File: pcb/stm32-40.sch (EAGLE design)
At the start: 83 parts, among them IC1 STM32F103RBT6, IC2 CAT24M01WI-GT3, IC3 MAX487-S, IC4 AMIS30663CANG2G, Q1 32768Hz, Q2 8MHz, SW1 KSS-2EG4430, SW2 KSS-2EG4430, X1 MCV3, X2 MCV3

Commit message: stamp + lcd
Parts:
- removed JP1: (no value), jtag:SWD-5_2.54
- removed STMP1: STAMP-40, stamp:STAMP-40
- added C13: 0.1, rc-master-smd:C_0603
- added LCD1: (no value), lcd1202:LCD1202-EXT
- added Q3: MMBT2222, semiconductor:MMBT2222
- added R37, R38, R39, R40, R43: 10, rc-master-smd:R_0603
- added R41, R42: 4.7K, rc-master-smd:R_0603
- added R44: 2K, rc-master-smd:R_0603
- added STMP2: STAMP-40, stamp:STAMP-40
- added SW3, SW4, SW5: KSS-2EG4430, buttons:KSS-2EG4430
- added SWD1: SWD-6, jtag:SWD-6
- G1: device battery:LI3VHOLDER -> battery:1220SMT
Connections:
- new net !LCD_CS: LCD1.!CS, R41.1
- new net BL: R44.2
- new net LCD_CLK: LCD1.SCLK
- new net LCD_DATA: LCD1.SI
- new net N$25: R37.1, STMP2G$1.6
- new net N$26: R38.1, STMP2G$1.5
- new net N$27: R39.1, STMP2G$1.4
- new net N$28: R40.1, STMP2G$1.3
- new net N$29: LCD1.LEDK, Q3.C
- new net N$31: LCD1.LEDA, R43.1
- new net N$32: Q3.B, R44.1
- new net PA15: IC1.JTDI/(TIM2_CH1_ETR/PA15/SPI1_NSS), STMP2G$2.4
- net !RESET: now also LCD1.!RST, R42.2, SWD1.5; no longer JP1.4
- net +3V3: now also C13.1, LCD1.VDD, LCD1.VDDI, R41.2, R43.2, SWD1.1; no longer JP1.1
- net +5V: now also STMP2G$1.1; no longer STMP1G$1.20
- net CAN_L: now also S1.8, X2.2.SK; no longer S1.1, X2.3.SK
- net GND: now also C13.2, LCD1.GND@3, LCD1.GND@8, Q3.E, R42.1, S1.5, S1.6, STMP2G$1.11, STMP2G$1.2, STMP2G$1.20, STMP2G$2.1, STMP2G$2.20, SW3.P, SW4.P, SW5.P, SWD1.3, X1.3.SK, X2.3.SK; no longer JP1.5, S1.3, S1.4, STMP1G$1.1, STMP1G$1.10, STMP1G$1.19, STMP1G$2.1, STMP1G$2.20, X1.2.SK, X2.2.SK
- net N$10: now also S1.4; no longer S1.5
- net N$11: now also STMP2G$1.10; no longer STMP1G$1.11
- net N$14: now also STMP2G$1.9; no longer STMP1G$1.12
- net N$15: now also STMP2G$1.19; no longer STMP1G$1.2
- net N$16: now also STMP2G$1.18; no longer STMP1G$1.3
- net N$17: now also STMP2G$1.17; no longer STMP1G$1.4
- net N$18: now also STMP2G$1.16; no longer STMP1G$1.5
- net N$19: now also STMP2G$1.15; no longer STMP1G$1.6
- net N$2: now also S1.1; no longer S1.8
- net N$20: now also STMP2G$1.14; no longer STMP1G$1.7
- net N$21: now also STMP2G$1.13; no longer STMP1G$1.8
- net N$22: now also STMP2G$1.12; no longer STMP1G$1.9
- net N$23: now also STMP2G$1.8; no longer STMP1G$1.13
- net N$24: now also STMP2G$1.7; no longer STMP1G$1.14
- net N$8: now also S1.2; no longer S1.7
- net N$9: now also S1.3; no longer S1.6
- net PA0: now also STMP2G$2.19; no longer STMP1G$2.2
- net PA1: now also STMP2G$2.18; no longer STMP1G$2.3
- net PA2: now also STMP2G$2.17; no longer STMP1G$2.4
- net PA3: now also STMP2G$2.16; no longer STMP1G$2.5
- net PA4: now also STMP2G$2.15; no longer STMP1G$2.6
- net PA5: now also STMP2G$2.14; no longer STMP1G$2.7
- net PA6: now also STMP2G$2.13; no longer STMP1G$2.8
- net PA7: now also STMP2G$2.12; no longer STMP1G$2.9
- net PA8: now also STMP2G$2.5
- net PB0: now also R39.2
- net PB1: now also R40.2
- net PC13: now also STMP2G$2.2; no longer STMP1G$2.19
- net PC4: now also R37.2
- net PC5: now also R38.2
- net PD2: now also STMP2G$2.3
- net RS485_A: now also X1.2.SK; no longer X1.1.SK
- net RS485_B: now also S1.7, X1.1.SK; no longer S1.2, X1.3.SK
- net SCL2: now also STMP2G$2.11
- net SDA2: now also STMP2G$2.10
- net SPI2_MISO: now also STMP2G$2.7
- net SPI2_MOSI: now also STMP2G$2.6
- net SPI2_NSS: now also STMP2G$2.9
- net SPI2_SCLK: now also STMP2G$2.8
- net SWCLK: now also SWD1.2; no longer JP1.3
- net SWDIO: now also SWD1.4; no longer JP1.2
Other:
- moved on the sheet: C1, C10, C11, C12, C2, C3, C4, C5, C6, C7, C8, C9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

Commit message: ...
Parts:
- added R45, R46: 200, rc-master-smd:R_0603
- R42: value 4.7K -> 200
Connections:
- removed net BL: R44.2
- net !LCD_CS: now also R46.2
- net !RESET: no longer R42.2
- net GND: no longer R42.1
- net LCD_CLK: now also R45.2
- net LCD_DATA: now also R42.2
- net PA1: now also R46.1
- net PA2: now also R42.1
- net PA4: now also R45.1
- net PD2: now also R44.2
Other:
- moved on the sheet: C13, LCD1, Q3, R41, R42, R43, R44, SW3, SW4, SW5

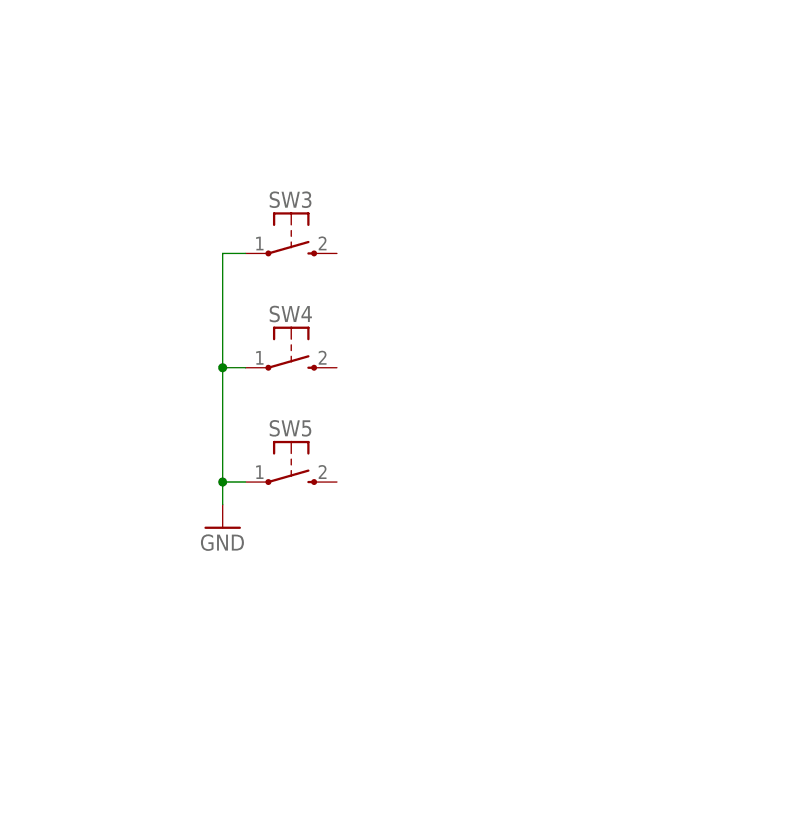
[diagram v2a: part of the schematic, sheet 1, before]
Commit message: 40 pin mesonine module done. Need check sch and pcb
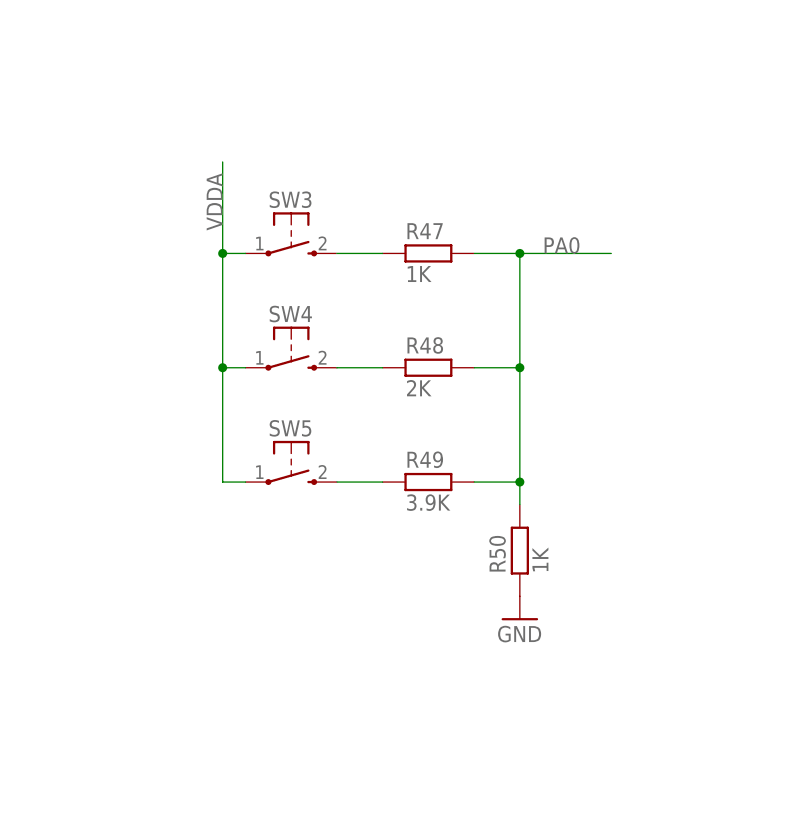
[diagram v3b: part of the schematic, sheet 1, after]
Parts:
- added R47, R50: 1K, rc-master-smd:R_0603
- added R48: 2K, rc-master-smd:R_0603
- added R49: 3.9K, rc-master-smd:R_0603
- renumbered STMP2 to STMP40
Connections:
- new net N$33: R47.1, SW3.S
- new net N$34: R48.1, SW4.S
- new net N$35: R49.1, SW5.S
- net GND: now also R50.1; no longer SW3.P, SW4.P, SW5.P
- net PA0: now also R47.2, R48.2, R49.2, R50.2
- net VDDA: now also SW3.P, SW4.P, SW5.P
